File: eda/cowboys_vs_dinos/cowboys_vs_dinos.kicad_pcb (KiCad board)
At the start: 2 copper layers, 122.5 x 218.8 mm, 1 part

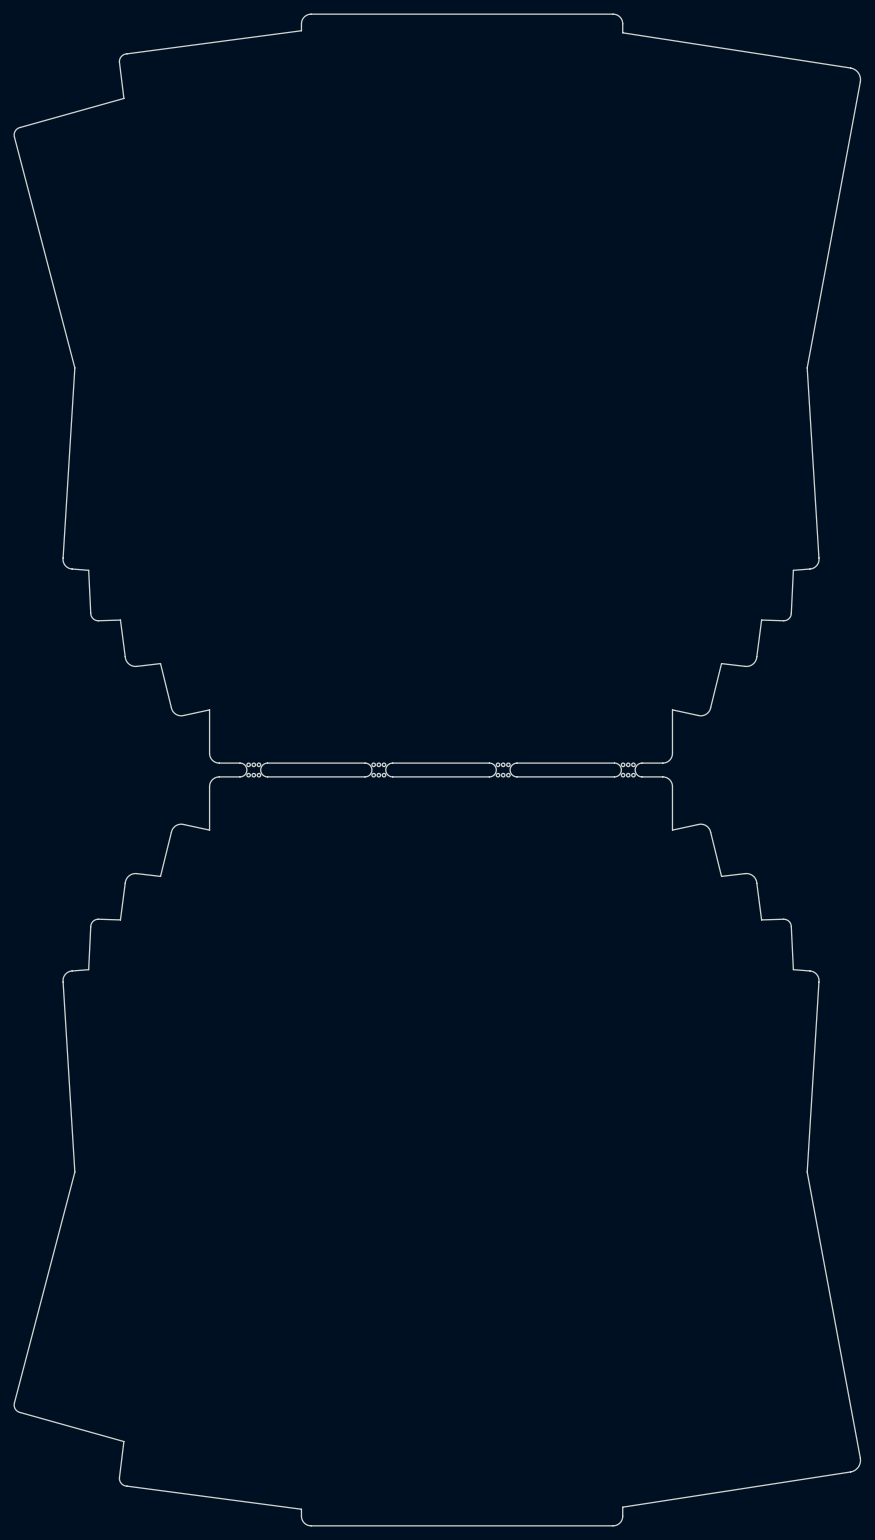
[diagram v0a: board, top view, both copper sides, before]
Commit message: art and pcb edge work
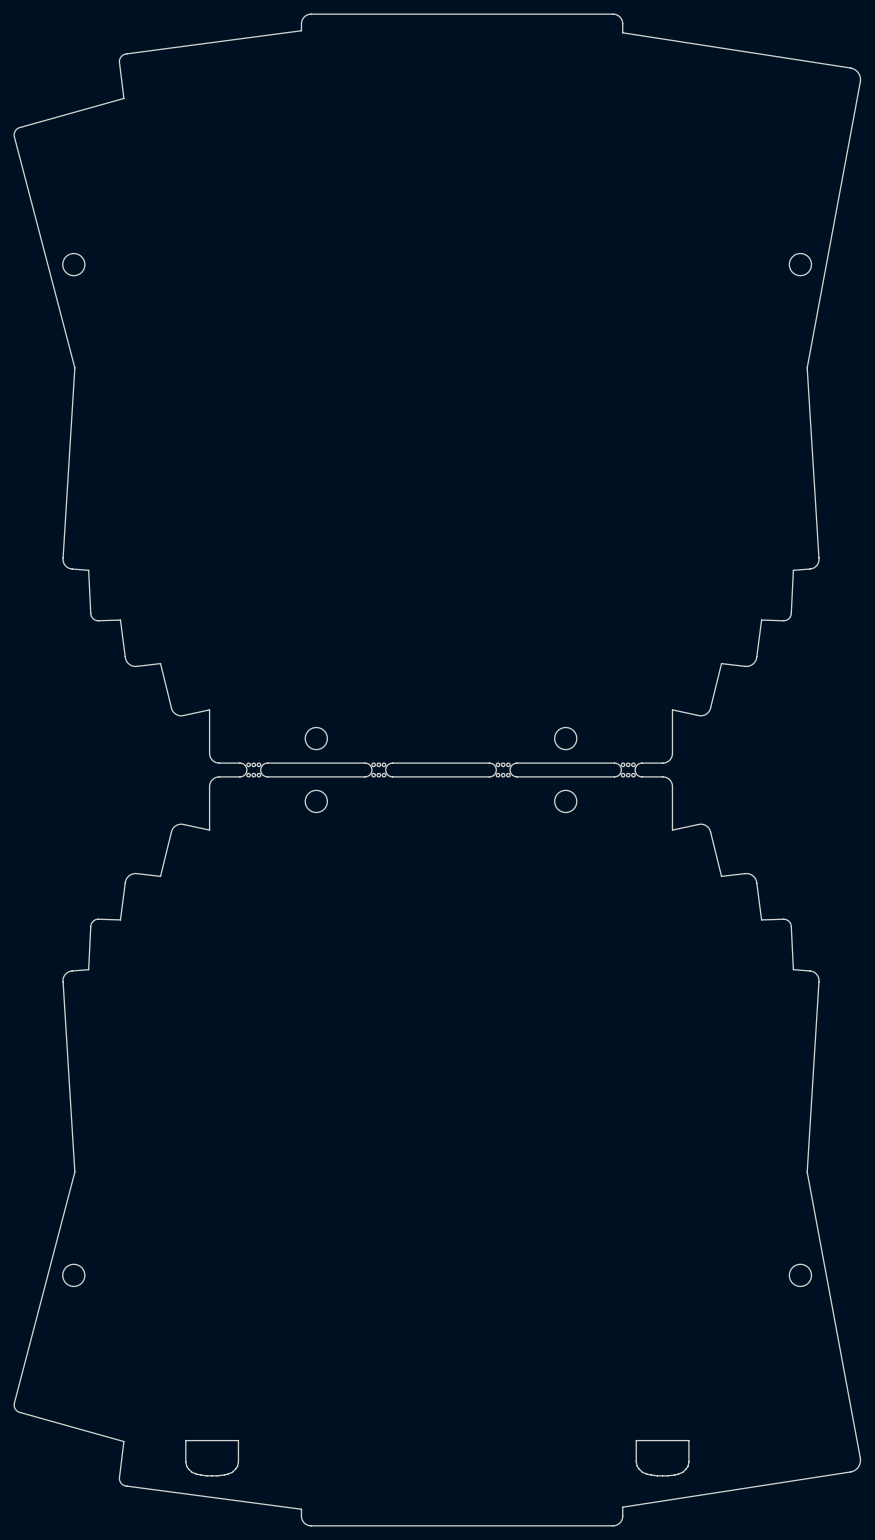
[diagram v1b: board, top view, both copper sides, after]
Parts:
- added Lanyard: Lanyard_Hole, 0_local:Lanyard_Hole, F.Cu at (75.0, 221.5)
- added Lanyard: Lanyard_Hole, 0_local:Lanyard_Hole, F.Cu at (140.2, 221.5)
- added REF**: 3.2mm_M3, 0_local:MountingHole_3.2mm_M3, F.Cu at (55.0, 49.0)
- added REF**: 3.2mm_M3, 0_local:MountingHole_3.2mm_M3, F.Cu at (160.2, 195.3)
- added REF**: 3.2mm_M3, 0_local:MountingHole_3.2mm_M3, F.Cu at (55.0, 195.3)
- added REF**: 3.2mm_M3, 0_local:MountingHole_3.2mm_M3, F.Cu at (160.2, 49.0)
- added REF**: 3.2mm_M3, 0_local:MountingHole_3.2mm_M3, F.Cu at (126.2, 117.6)
- added REF**: 3.2mm_M3, 0_local:MountingHole_3.2mm_M3, F.Cu at (90.1, 126.7)
- added REF**: 3.2mm_M3, 0_local:MountingHole_3.2mm_M3, F.Cu at (126.2, 126.7)
- added REF**: 3.2mm_M3, 0_local:MountingHole_3.2mm_M3, F.Cu at (90.1, 117.6)
